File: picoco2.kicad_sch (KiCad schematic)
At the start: 41 parts, among them J1 Conn_01x03_Female, J2 Micro_SD_Card, J3 Conn_01x03_Female, Q1 Q_NMOS_GDS, SW1 SW_Push, SW2 SW_Push, U1 PicoW, U2 scd30, U3 ssd1306, U4 PCF8523T, U5 MCP73831-2-OT, Y1 Crystal_GND23

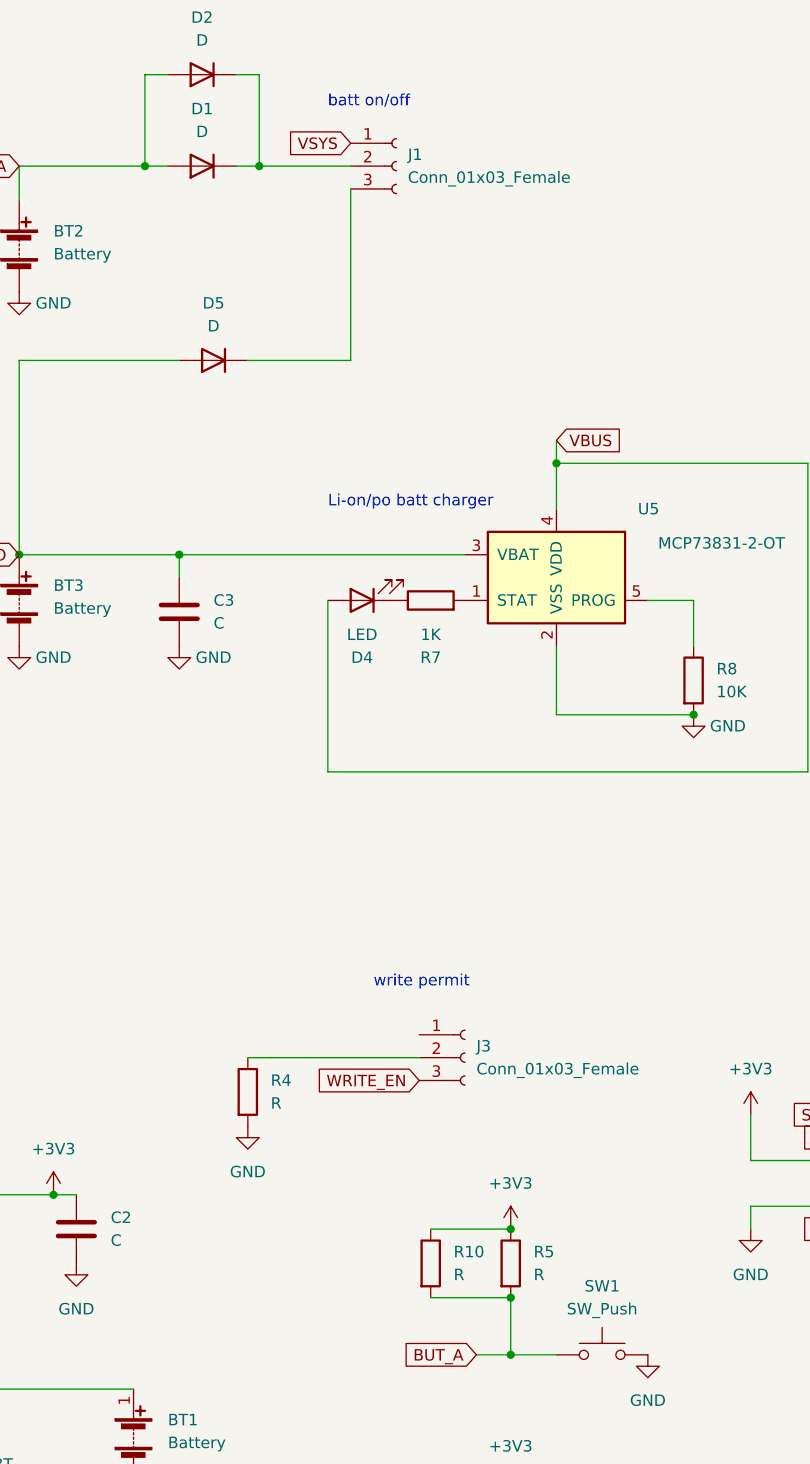
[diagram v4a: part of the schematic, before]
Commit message: routed power lines
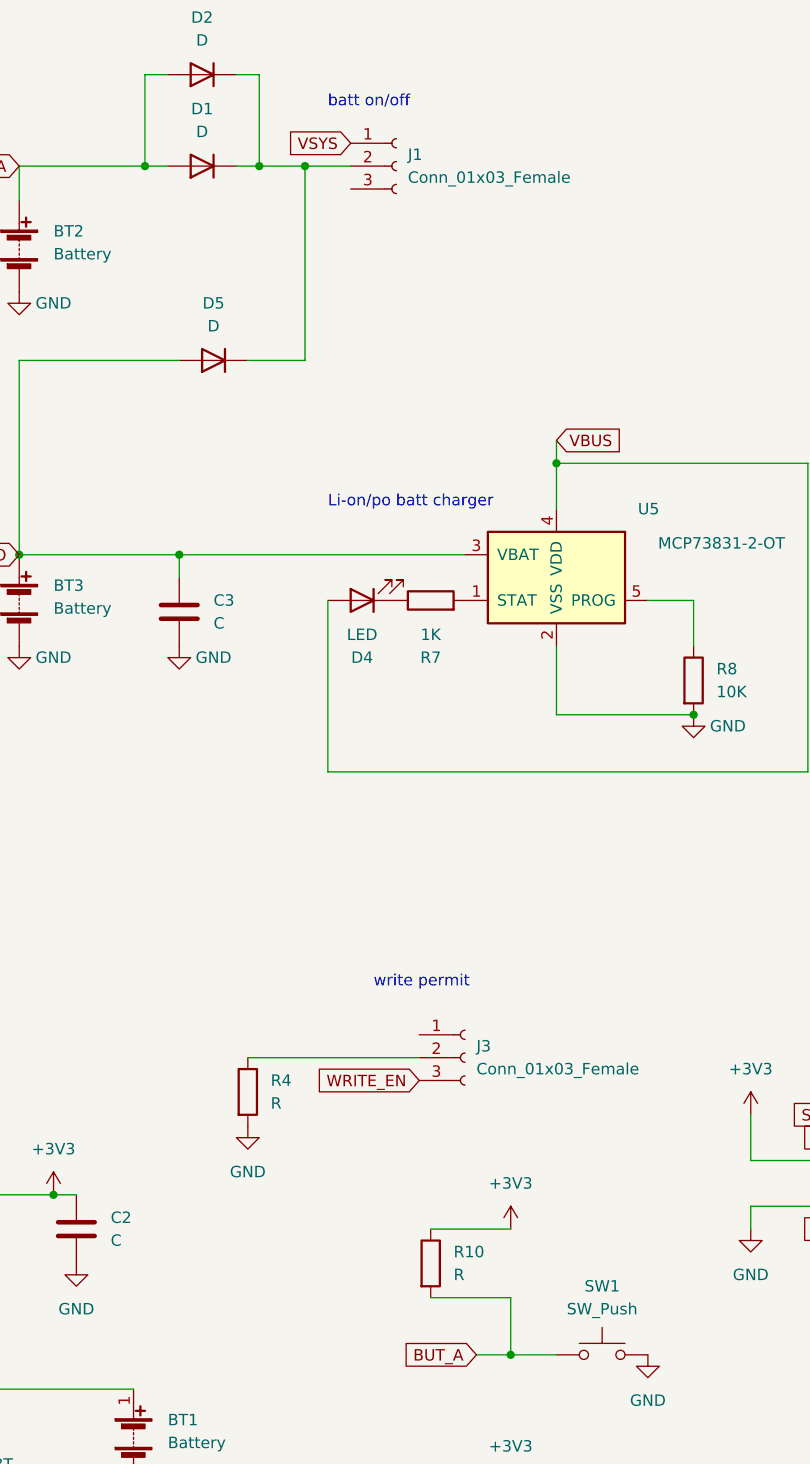
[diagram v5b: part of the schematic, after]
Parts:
- removed R5: R, Resistor_SMD:R_0603_1608Metric_Pad0.98x0.95mm_HandSolder, symbol Device:R
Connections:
- net at D1.1 (K), D2.1 (K), J1.2 (Pin_2): now also D5.1 (K)
- net at J1.3 (Pin_3): no longer D5.1 (K)
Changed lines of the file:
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@@
   (junction (at 134.62 185.42) (diameter 0) (color 0 0 0 0)
   )
-  (junction (at 134.62 148.59) (diameter 0) (color 0 0 0 0)
-  )
   (junction (at 247.65 157.48) (diameter 0) (color 0 0 0 0)
   )
   (junction (at 93.98 30.48) (diameter 0) (color 0 0 0 0)
   )
-  (junction (at 134.62 156.21) (diameter 0) (color 0 0 0 0)
-  )
   (junction (at 39.37 43.18) (diameter 0) (color 0 0 0 0)
   )
+  (junction (at 111.76 30.48) (diameter 0) (color 0 0 0 0)
+  )
   (junction (at 83.82 144.78) (diameter 0) (color 0 0 0 0)
   )
@@
     (stroke (width 0) (type default) (color 0 0 0 0))
   )
-  (wire (pts (xy 105.41 52.07) (xy 116.84 52.07))
-    (stroke (width 0) (type default) (color 0 0 0 0))
-  )
   (wire (pts (xy 173.99 140.97) (xy 161.29 140.97))
     (stroke (width 0) (type default) (color 0 0 0 0))
@@
     (stroke (width 0) (type default) (color 0 0 0 0))
   )
-  (wire (pts (xy 106.68 30.48) (xy 116.84 30.48))
+  (wire (pts (xy 106.68 30.48) (xy 111.76 30.48))
     (stroke (width 0) (type default) (color 0 0 0 0))
   )
@@
     (stroke (width 0) (type default) (color 0 0 0 0))
   )
+  (wire (pts (xy 105.41 52.07) (xy 111.76 52.07))
+    (stroke (width 0) (type default) (color 0 0 0 0))
+  )
   (wire (pts (xy 34.29 179.07) (xy 34.29 180.34))
     (stroke (width 0) (type default) (color 0 0 0 0))
@@
     (stroke (width 0) (type default) (color 0 0 0 0))
   )
+  (wire (pts (xy 111.76 52.07) (xy 111.76 30.48))
+    (stroke (width 0) (type default) (color 0 0 0 0))
+  )
   (wire (pts (xy 25.4 114.3) (xy 25.4 119.38))
     (stroke (width 0) (type default) (color 0 0 0 0))
@@
     (stroke (width 0) (type default) (color 0 0 0 0))
   )
+  (wire (pts (xy 111.76 30.48) (xy 116.84 30.48))
+    (stroke (width 0) (type default) (color 0 0 0 0))
+  )
   (wire (pts (xy 39.37 35.56) (xy 48.26 35.56))
     (stroke (width 0) (type default) (color 0 0 0 0))
@@
   )
   (wire (pts (xy 139.7 60.96) (xy 139.7 63.5))
-    (stroke (width 0) (type default) (color 0 0 0 0))
-  )
-  (wire (pts (xy 116.84 33.02) (xy 116.84 52.07))
     (stroke (width 0) (type default) (color 0 0 0 0))
   )
@@
     (pin "1")
   )
-  (symbol (lib_id "Device:R") (at 134.62 152.4 0) (unit 1)
-    (in_bom yes) (on_board yes) (fields_autoplaced)
-    (property "Reference" "R5" (id 0) (at 137.16 151.1299 0)
-      (effects (font (size 1.27 1.27)) (justify left))
-    )
-    (property "Value" "R" (id 1) (at 137.16 153.6699 0)
-      (effects (font (size 1.27 1.27)) (justify left))
-    )
-    (property "Footprint" "Resistor_SMD:R_0603_1608Metric_Pad0.98x0.95mm_HandSolder" (id 2) (at 132.842 152.4 90)
-      (effects (font (size 1.27 1.27)) hide)
-    )
-    (property "Datasheet" "~" (id 3) (at 134.62 152.4 0)
-      (effects (font (size 1.27 1.27)) hide)
-    )
-    (pin "1")
-    (pin "2")
-  )
   (symbol (lib_id "power:+3V3") (at 31.75 35.56 0) (unit 1)
     (in_bom yes) (on_board yes) (fields_autoplaced)
@@
       (reference "R4") (unit 1) (value "R") (footprint "Resistor_SMD:R_0603_1608Metric_Pad0.98x0.95mm_HandSolder")
     )
-    (path "/ed312207-38ff-4d59-b501-cd47b1e8e31f"
-      (reference "R5") (unit 1) (value "R") (footprint "Resistor_SMD:R_0603_1608Metric_Pad0.98x0.95mm_HandSolder")
-    )
     (path "/70b9d360-ae9d-4d05-9551-d48f9ad2704c"

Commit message: full routing
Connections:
- net SCL: no longer U3.4 (SDA)
- net SDA: now also U3.4 (SDA)
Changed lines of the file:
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@@
     )
   )
-  (global_label "SCL" (shape input) (at 45.72 118.11 0) (fields_autoplaced)
+  (global_label "SDA" (shape input) (at 45.72 118.11 0) (fields_autoplaced)
     (effects (font (size 1.27 1.27)) (justify left))
-    (property "Intersheet References" "${INTERSHEET_REFS}" (id 0) (at 51.6407 118.1894 0)
+    (property "Intersheet References" "${INTERSHEET_REFS}" (id 0) (at 51.7012 118.0306 0)
       (effects (font (size 1.27 1.27)) (justify left) hide)
     )

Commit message: updated values on components
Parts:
- BT1: value Battery -> CR1220
- C1, C2, C3: value C -> 10uF
- R1, R12, R13, R2: value R -> 4.7K
- R10, R11, R3, R9: value R -> 10K
- R6: value R -> 1K
- Y1: value Crystal_GND23 -> 32KHz
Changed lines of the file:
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@@
       (effects (font (size 1.27 1.27)) (justify left))
     )
-    (property "Value" "R" (id 1) (at 128.27 182.8799 0)
+    (property "Value" "10K" (id 1) (at 128.27 182.8799 0)
       (effects (font (size 1.27 1.27)) (justify left))
     )
@@
     (in_bom yes) (on_board yes)
     (property "Reference" "Y1" (id 0) (at 46.99 179.451 90))
-    (property "Value" "Crystal_GND23" (id 1) (at 20.32 182.88 90))
+    (property "Value" "32KHz" (id 1) (at 20.32 182.88 90))
     (property "Footprint" "Crystal:Crystal_SMD_Abracon_ABS25-4Pin_8.0x3.8mm" (id 2) (at 34.29 184.15 0)
       (effects (font (size 1.27 1.27)) hide)
@@
       (effects (font (size 1.27 1.27)) (justify left))
     )
-    (property "Value" "Battery" (id 1) (at 96.52 172.3389 0)
+    (property "Value" "CR1220" (id 1) (at 96.52 172.3389 0)
       (effects (font (size 1.27 1.27)) (justify left))
     )
@@
       (effects (font (size 1.27 1.27)) (justify left))
     )
-    (property "Value" "C" (id 1) (at 66.04 149.8599 0)
+    (property "Value" "10uF" (id 1) (at 66.04 149.8599 0)
       (effects (font (size 1.27 1.27)) (justify left))
     )
@@
       (effects (font (size 1.27 1.27)) (justify left))
     )
-    (property "Value" "R" (id 1) (at 41.91 40.6399 0)
+    (property "Value" "4.7K" (id 1) (at 41.91 40.6399 0)
       (effects (font (size 1.27 1.27)) (justify left))
     )
@@
       (effects (font (size 1.27 1.27)) (justify left))
     )
-    (property "Value" "R" (id 1) (at 26.67 40.6399 0)
+    (property "Value" "4.7K" (id 1) (at 26.67 40.6399 0)
       (effects (font (size 1.27 1.27)) (justify left))
     )
@@
       (effects (font (size 1.27 1.27)) (justify left))
     )
-    (property "Value" "R" (id 1) (at 34.29 40.6399 0)
+    (property "Value" "4.7K" (id 1) (at 34.29 40.6399 0)
       (effects (font (size 1.27 1.27)) (justify left))
     )
@@
       (effects (font (size 1.27 1.27)) (justify left))
     )
-    (property "Value" "R" (id 1) (at 50.8 40.6399 0)
+    (property "Value" "4.7K" (id 1) (at 50.8 40.6399 0)
       (effects (font (size 1.27 1.27)) (justify left))
     )
@@
       (effects (font (size 1.27 1.27)) (justify left))
     )
-    (property "Value" "C" (id 1) (at 90.17 149.8599 0)
+    (property "Value" "10uF" (id 1) (at 90.17 149.8599 0)
       (effects (font (size 1.27 1.27)) (justify left))
     )
@@
     (in_bom yes) (on_board yes) (fields_autoplaced)
     (property "Reference" "R6" (id 0) (at 73.66 138.43 90))
-    (property "Value" "R" (id 1) (at 73.66 140.97 90))
+    (property "Value" "1K" (id 1) (at 73.66 140.97 90))
     (property "Footprint" "Resistor_SMD:R_0603_1608Metric_Pad0.98x0.95mm_HandSolder" (id 2) (at 73.66 146.558 90)
       (effects (font (size 1.27 1.27)) hide)
@@
       (effects (font (size 1.27 1.27)) (justify left))
     )
-    (property "Value" "R" (id 1) (at 250.19 154.9399 0)
+    (property "Value" "10K" (id 1) (at 250.19 154.9399 0)
       (effects (font (size 1.27 1.27)) (justify left))
     )
@@
       (effects (font (size 1.27 1.27)) (justify left))
     )
-    (property "Value" "R" (id 1) (at 137.16 182.8799 0)
+    (property "Value" "10K" (id 1) (at 137.16 182.8799 0)
       (effects (font (size 1.27 1.27)) (justify left))
     )
@@
       (effects (font (size 1.27 1.27)) (justify left))
     )
-    (property "Value" "R" (id 1) (at 128.27 153.6699 0)
+    (property "Value" "10K" (id 1) (at 128.27 153.6699 0)
       (effects (font (size 1.27 1.27)) (justify left))
     )
@@
       (effects (font (size 1.27 1.27)) (justify left))
     )
-    (property "Value" "C" (id 1) (at 101.6 81.2799 0)
+    (property "Value" "10uF" (id 1) (at 101.6 81.2799 0)
       (effects (font (size 1.27 1.27)) (justify left))
     )
@@
     )
     (path "/223af7cc-a0d5-4e22-9574-6b9ea27ce9a0"
-      (reference "BT1") (unit 1) (value "Battery") (footprint "picoco2:CR1220-2")
+      (reference "BT1") (unit 1) (value "CR1220") (footprint "picoco2:CR1220-2")
     )
     (path "/dea8c086-3176-4223-947b-b11dc0a0cc23"
@@
     )
     (path "/22f77696-af2a-45c1-817a-3091b36e49f1"
-      (reference "C1") (unit 1) (value "C") (footprint "Capacitor_SMD:C_0603_1608Metric_Pad1.08x0.95mm_HandSolder")
+      (reference "C1") (unit 1) (value "10uF") (footprint "Capacitor_SMD:C_0603_1608Metric_Pad1.08x0.95mm_HandSolder")
     )
     (path "/65182113-2c24-434c-b991-060d822d7776"
-      (reference "C2") (unit 1) (value "C") (footprint "Capacitor_SMD:C_0603_1608Metric_Pad1.08x0.95mm_HandSolder")
+      (reference "C2") (unit 1) (value "10uF") (footprint "Capacitor_SMD:C_0603_1608Metric_Pad1.08x0.95mm_HandSolder")
     )
     (path "/fdb966f1-cd49-4e3a-b3c7-28a5874dad3c"
-      (reference "C3") (unit 1) (value "C") (footprint "Capacitor_SMD:C_0603_1608Metric_Pad1.08x0.95mm_HandSolder")
+      (reference "C3") (unit 1) (value "10uF") (footprint "Capacitor_SMD:C_0603_1608Metric_Pad1.08x0.95mm_HandSolder")
     )
     (path "/903eb955-6b36-4f1d-b456-775556e29b53"
@@
     )
     (path "/44b88ca8-1512-4e24-b4a6-680b185f6b9a"
-      (reference "R1") (unit 1) (value "R") (footprint "Resistor_SMD:R_0603_1608Metric_Pad0.98x0.95mm_HandSolder")
+      (reference "R1") (unit 1) (value "4.7K") (footprint "Resistor_SMD:R_0603_1608Metric_Pad0.98x0.95mm_HandSolder")
     )
     (path "/3c38f3ba-cae9-4e7a-9786-dd4393cfdb98"
-      (reference "R2") (unit 1) (value "R") (footprint "Resistor_SMD:R_0603_1608Metric_Pad0.98x0.95mm_HandSolder")
+      (reference "R2") (unit 1) (value "4.7K") (footprint "Resistor_SMD:R_0603_1608Metric_Pad0.98x0.95mm_HandSolder")
     )
     (path "/77d2fa6f-7625-46da-b762-d8eaeebbf159"
-      (reference "R3") (unit 1) (value "R") (footprint "Resistor_SMD:R_0603_1608Metric_Pad0.98x0.95mm_HandSolder")
+      (reference "R3") (unit 1) (value "10K") (footprint "Resistor_SMD:R_0603_1608Metric_Pad0.98x0.95mm_HandSolder")
     )
     (path "/9c5c4ab5-8c1c-47fe-a830-9c832d0c9d03"
@@
     )
     (path "/70b9d360-ae9d-4d05-9551-d48f9ad2704c"
-      (reference "R6") (unit 1) (value "R") (footprint "Resistor_SMD:R_0603_1608Metric_Pad0.98x0.95mm_HandSolder")
+      (reference "R6") (unit 1) (value "1K") (footprint "Resistor_SMD:R_0603_1608Metric_Pad0.98x0.95mm_HandSolder")
     )
     (path "/21b383ef-508b-4fa4-939e-dace4ed3f133"
@@
     )
     (path "/98b38059-616b-4cc4-8124-6e430561f957"
-      (reference "R9") (unit 1) (value "R") (footprint "Resistor_SMD:R_0603_1608Metric_Pad0.98x0.95mm_HandSolder")
+      (reference "R9") (unit 1) (value "10K") (footprint "Resistor_SMD:R_0603_1608Metric_Pad0.98x0.95mm_HandSolder")
     )
     (path "/9da05190-9384-42de-a941-67e08d99ea41"
-      (reference "R10") (unit 1) (value "R") (footprint "Resistor_THT:R_Axial_DIN0204_L3.6mm_D1.6mm_P7.62mm_Horizontal")
+      (reference "R10") (unit 1) (value "10K") (footprint "Resistor_THT:R_Axial_DIN0204_L3.6mm_D1.6mm_P7.62mm_Horizontal")
     )
     (path "/06c4a90f-880c-45bf-bd61-4a14853078f1"
-      (reference "R11") (unit 1) (value "R") (footprint "Resistor_THT:R_Axial_DIN0204_L3.6mm_D1.6mm_P7.62mm_Horizontal")
+      (reference "R11") (unit 1) (value "10K") (footprint "Resistor_THT:R_Axial_DIN0204_L3.6mm_D1.6mm_P7.62mm_Horizontal")
     )
     (path "/4011fa0e-48f5-4fd9-9370-a57a889afe66"
-      (reference "R12") (unit 1) (value "R") (footprint "Resistor_THT:R_Axial_DIN0204_L3.6mm_D1.6mm_P7.62mm_Horizontal")
+      (reference "R12") (unit 1) (value "4.7K") (footprint "Resistor_THT:R_Axial_DIN0204_L3.6mm_D1.6mm_P7.62mm_Horizontal")
     )
     (path "/4c8c89b2-38a6-41c6-bd98-2803ad9fa73c"
-      (reference "R13") (unit 1) (value "R") (footprint "Resistor_THT:R_Axial_DIN0204_L3.6mm_D1.6mm_P7.62mm_Horizontal")
+      (reference "R13") (unit 1) (value "4.7K") (footprint "Resistor_THT:R_Axial_DIN0204_L3.6mm_D1.6mm_P7.62mm_Horizontal")
     )
     (path "/d3fbd5d9-edde-42e2-941e-f1cb0af1d541"
@@
     )
     (path "/10a1db89-770e-405f-8c89-c397f2f7158e"
-      (reference "Y1") (unit 1) (value "Crystal_GND23") (footprint "Crystal:Crystal_SMD_Abracon_ABS25-4Pin_8.0x3.8mm")
-    )
-  )
+      (reference "Y1") (unit 1) (value "32KHz") (footprint "Crystal:Crystal_SMD_Abracon_ABS25-4Pin_8.0x3.8mm")
+    )
+  )
